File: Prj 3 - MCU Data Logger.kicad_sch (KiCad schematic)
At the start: 25 parts, among them U1 24LC1025, U2 24LC1025, U3 DS1337S_, U4 ATMEGA328P-AU, Y1 32.768 KHz, Y2 16MHz

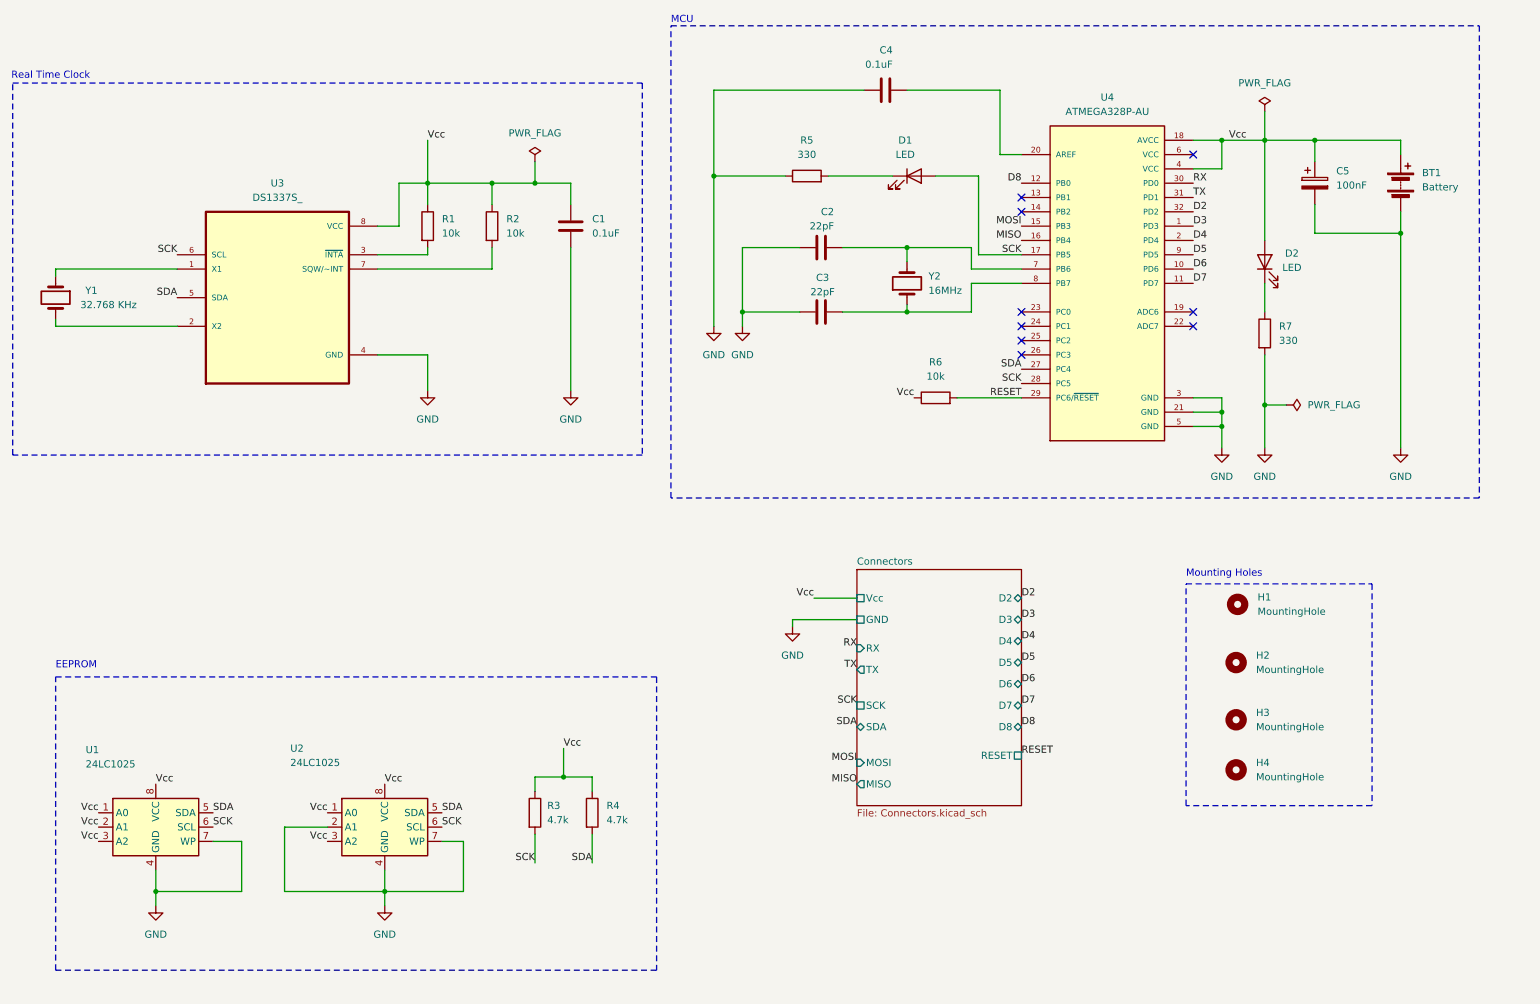
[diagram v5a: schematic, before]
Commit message: fixed 2 defects in schematic
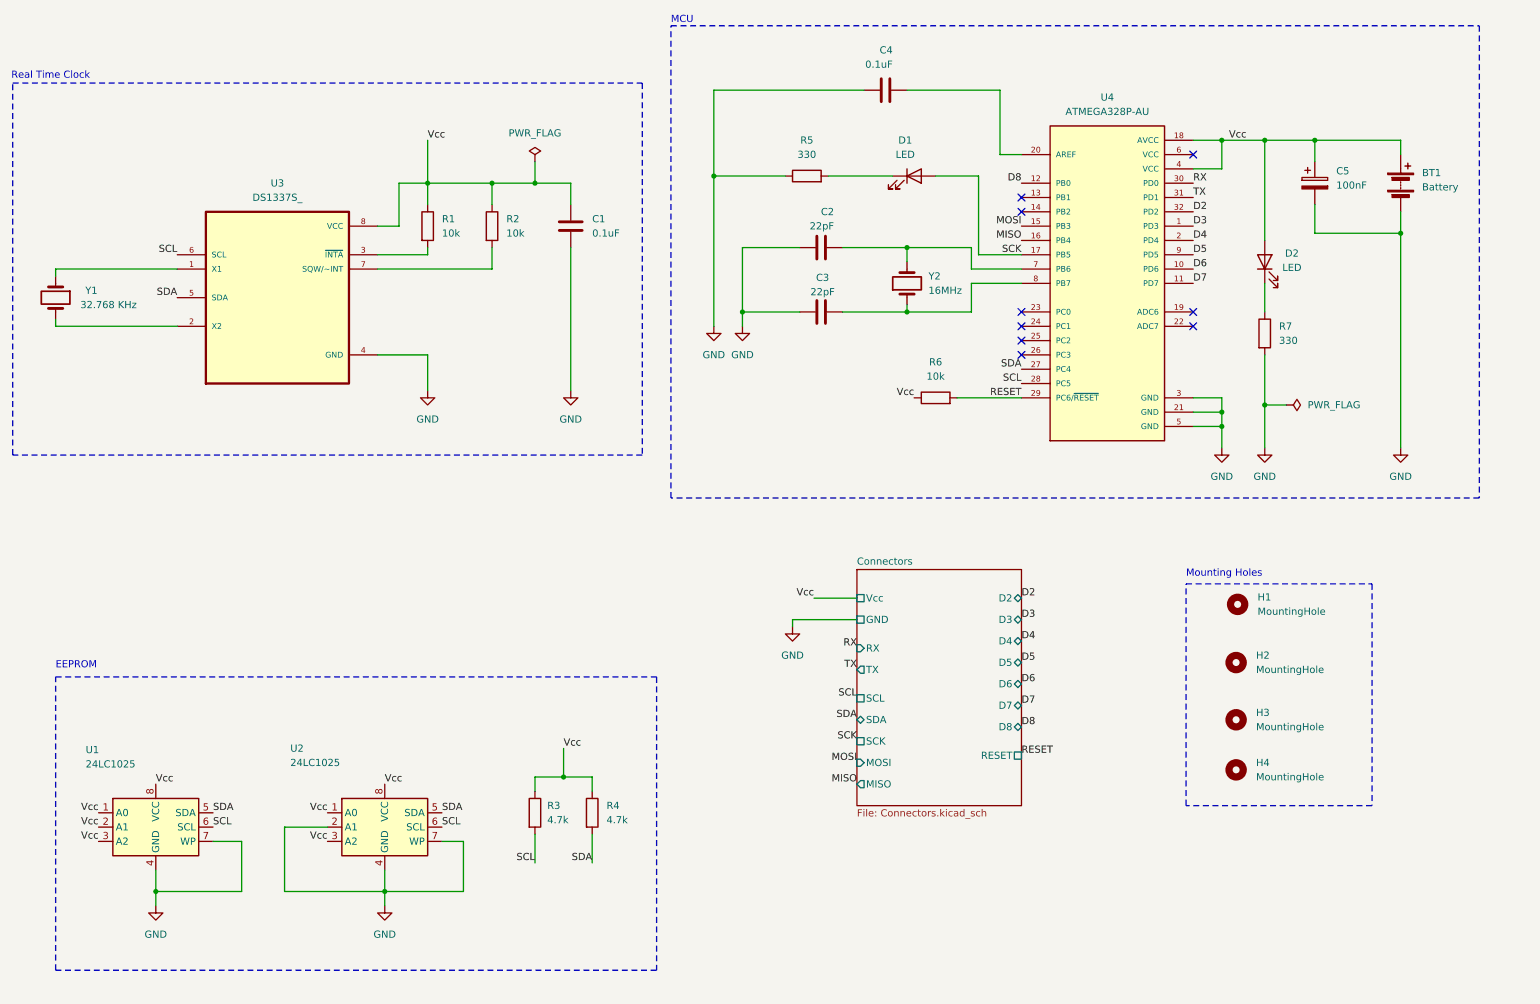
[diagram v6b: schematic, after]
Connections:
- net SCK: no longer R3.2, U1.6 (SCL), U2.6 (SCL), U3.6 (SCL), U4.28 (PC5)
- new net SCL: R3.2, U1.6 (SCL), U2.6 (SCL), U3.6 (SCL), U4.28 (PC5)
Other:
- sheet Connectors ports: added SCL; removed none
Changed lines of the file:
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@@
 	(wire
 		(pts
-			(xy 238.76 33.02) (xy 238.76 38.1)
-		)
-		(stroke
-			(width 0)
-			(type default)
-		)
-	)
-	(wire
-		(pts
 			(xy 163.83 57.15) (xy 175.26 57.15)
 		)
@@
 		)
 	)
-	(label "SCK"
+	(label "SCL"
 		(at 92.71 160.02 0)
 		(fields_autoplaced yes)
@@
 		)
 	)
-	(label "SCK"
+	(label "SCL"
 		(at 109.22 166.37 180)
 		(fields_autoplaced yes)
@@
 		)
 	)
+	(label "SCK"
+		(at 166.37 144.78 180)
+		(fields_autoplaced yes)
+		(effects
+			(font
+				(size 1.27 1.27)
+			)
+			(justify right bottom)
+		)
+	)
 	(label "Vcc"
 		(at 72.39 157.48 180)
@@
 		)
 	)
-	(label "SCK"
+	(label "SCL"
 		(at 45.72 58.42 180)
 		(fields_autoplaced yes)
@@
 		)
 	)
-	(label "SCK"
+	(label "SCL"
 		(at 195.58 81.28 180)
 		(fields_autoplaced yes)
@@
 	)
 	(label "SDA"
-		(at 166.37 142.24 180)
+		(at 166.37 140.97 180)
 		(fields_autoplaced yes)
 		(effects
@@
 		)
 	)
-	(label "SCK"
-		(at 166.37 138.43 180)
+	(label "SCL"
+		(at 166.37 137.16 180)
 		(fields_autoplaced yes)
 		(effects
@@
 		)
 	)
-	(label "SCK"
+	(label "SCL"
 		(at 52.07 160.02 0)
 		(fields_autoplaced yes)
@@
 	)
 	(symbol
-		(lib_id "power:PWR_FLAG")
-		(at 238.76 33.02 0)
-		(unit 1)
-		(exclude_from_sim no)
-		(in_bom yes)
-		(on_board yes)
-		(dnp no)
-		(fields_autoplaced yes)
-		(property "Reference" "#FLG01"
-			(at 238.76 31.115 0)
-			(effects
-				(font
-					(size 1.27 1.27)
-				)
-				(hide yes)
-			)
-		)
-		(property "Value" "PWR_FLAG"
-			(at 238.76 27.94 0)
-			(effects
-				(font
-					(size 1.27 1.27)
-				)
-			)
-		)
-		(property "Footprint" ""
-			(at 238.76 33.02 0)
-			(effects
-				(font
-					(size 1.27 1.27)
-				)
-				(hide yes)
-			)
-		)
-		(property "Datasheet" "~"
-			(at 238.76 33.02 0)
-			(effects
-				(font
-					(size 1.27 1.27)
-				)
-				(hide yes)
-			)
-		)
-		(property "Description" "Special symbol for telling ERC where power comes from"
-			(at 238.76 33.02 0)
-			(effects
-				(font
-					(size 1.27 1.27)
-				)
-				(hide yes)
-			)
-		)
-		(pin "1"
-		)
-		(instances
-			(project "Prj 3 - MCU Data Logger"
-				(path "/195cc2ab-a3ee-4376-8389-6a32fc3c9724"
-					(reference "#FLG01")
-					(unit 1)
-				)
-			)
-		)
-	)
-	(symbol
 		(lib_id "Device:R")
 		(at 180.34 83.82 90)
@@
 			)
 		)
-		(pin "SCK" passive
-			(at 166.37 138.43 180)
-			(effects
-				(font
-					(size 1.27 1.27)
-				)
-				(justify left)
-			)
-		)
 		(pin "SDA" bidirectional
-			(at 166.37 142.24 180)
+			(at 166.37 140.97 180)
 			(effects
 				(font
@@
 			)
 		)
+		(pin "SCL" passive
+			(at 166.37 137.16 180)
+			(effects
+				(font
+					(size 1.27 1.27)
+				)
+				(justify left)
+			)
+		)
+		(pin "SCK" passive
+			(at 166.37 144.78 180)
+			(effects
+				(font
+					(size 1.27 1.27)
+				)
+				(justify left)
+			)
+		)
